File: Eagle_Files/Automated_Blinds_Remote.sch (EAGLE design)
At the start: 25 parts, among them U1 LPC1114FN28/102, U2 UA78MC

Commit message: Finished PCB design for remote control
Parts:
- added R8, R9: 10, rcl:R-US_0207/10
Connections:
- net +3V3: now also R8.2, R9.2
- net N$1: now also R8.1, R9.1
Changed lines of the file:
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@@
 <part name="+3V14" library="supply1" deviceset="+3V3" device=""/>
 <part name="POWER_SWITCH" library="DIP-SLIDE-SWITCH_3P-11.6X4.0X5.4_2.0MM_" deviceset="DIP-SLIDE-SWITCH(3P-11.6X4.0X5.4+2.0MM)" device="-EG1218"/>
+<part name="R8" library="rcl" deviceset="R-US_" device="0207/10" value="10"/>
+<part name="R9" library="rcl" deviceset="R-US_" device="0207/10" value="10"/>
 </parts>
 <sheets>
@@
 <text x="-55.88" y="73.66" size="1.778" layer="91">ACTION BUTTONS</text>
 <text x="-55.88" y="15.24" size="1.778" layer="91">SELECTION BUTTONS</text>
-<text x="78.74" y="96.52" size="1.778" layer="91">IR TRANSMITTER</text>
+<text x="68.58" y="96.52" size="1.778" layer="91">IR TRANSMITTER</text>
 </plain>
 <instances>
@@
 <instance part="+3V14" gate="G$1" x="86.36" y="91.44"/>
 <instance part="POWER_SWITCH" gate="G$1" x="22.86" y="68.58"/>
+<instance part="R8" gate="G$1" x="96.52" y="78.74" rot="MR0"/>
+<instance part="R9" gate="G$1" x="96.52" y="93.98" rot="MR0"/>
 </instances>
 <busses>
@@
 <wire x1="86.36" y1="86.36" x2="86.36" y2="88.9" width="0.1524" layer="91"/>
 <pinref part="+3V14" gate="G$1" pin="+3V3"/>
+<pinref part="R9" gate="G$1" pin="2"/>
+<wire x1="91.44" y1="86.36" x2="91.44" y2="93.98" width="0.1524" layer="91"/>
+<pinref part="R8" gate="G$1" pin="2"/>
+<wire x1="91.44" y1="86.36" x2="91.44" y2="78.74" width="0.1524" layer="91"/>
 </segment>
 </net>
@@
 <pinref part="R7" gate="G$1" pin="1"/>
 <wire x1="106.68" y1="86.36" x2="101.6" y2="86.36" width="0.1524" layer="91"/>
-</segment>
-</net>
+<pinref part="R8" gate="G$1" pin="1"/>
+<wire x1="101.6" y1="78.74" x2="101.6" y2="86.36" width="0.1524" layer="91"/>
+<pinref part="R9" gate="G$1" pin="1"/>
+<wire x1="101.6" y1="93.98" x2="101.6" y2="86.36" width="0.1524" layer="91"/>
+</segment>
+</net>

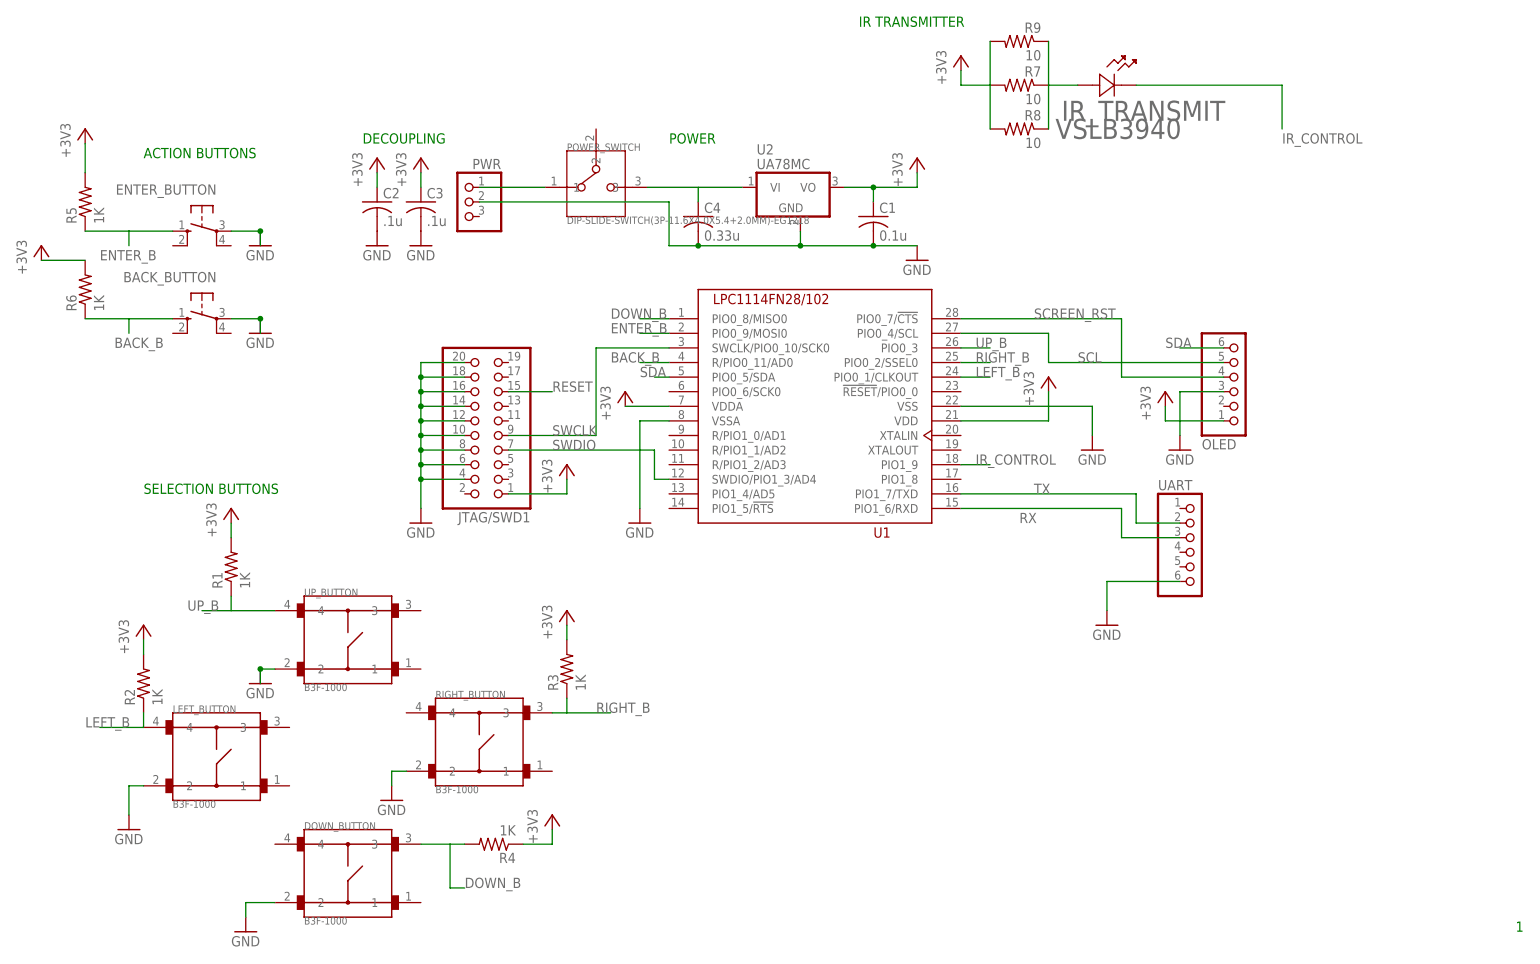
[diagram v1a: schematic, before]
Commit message: Updated value of button pull-ups in schematic
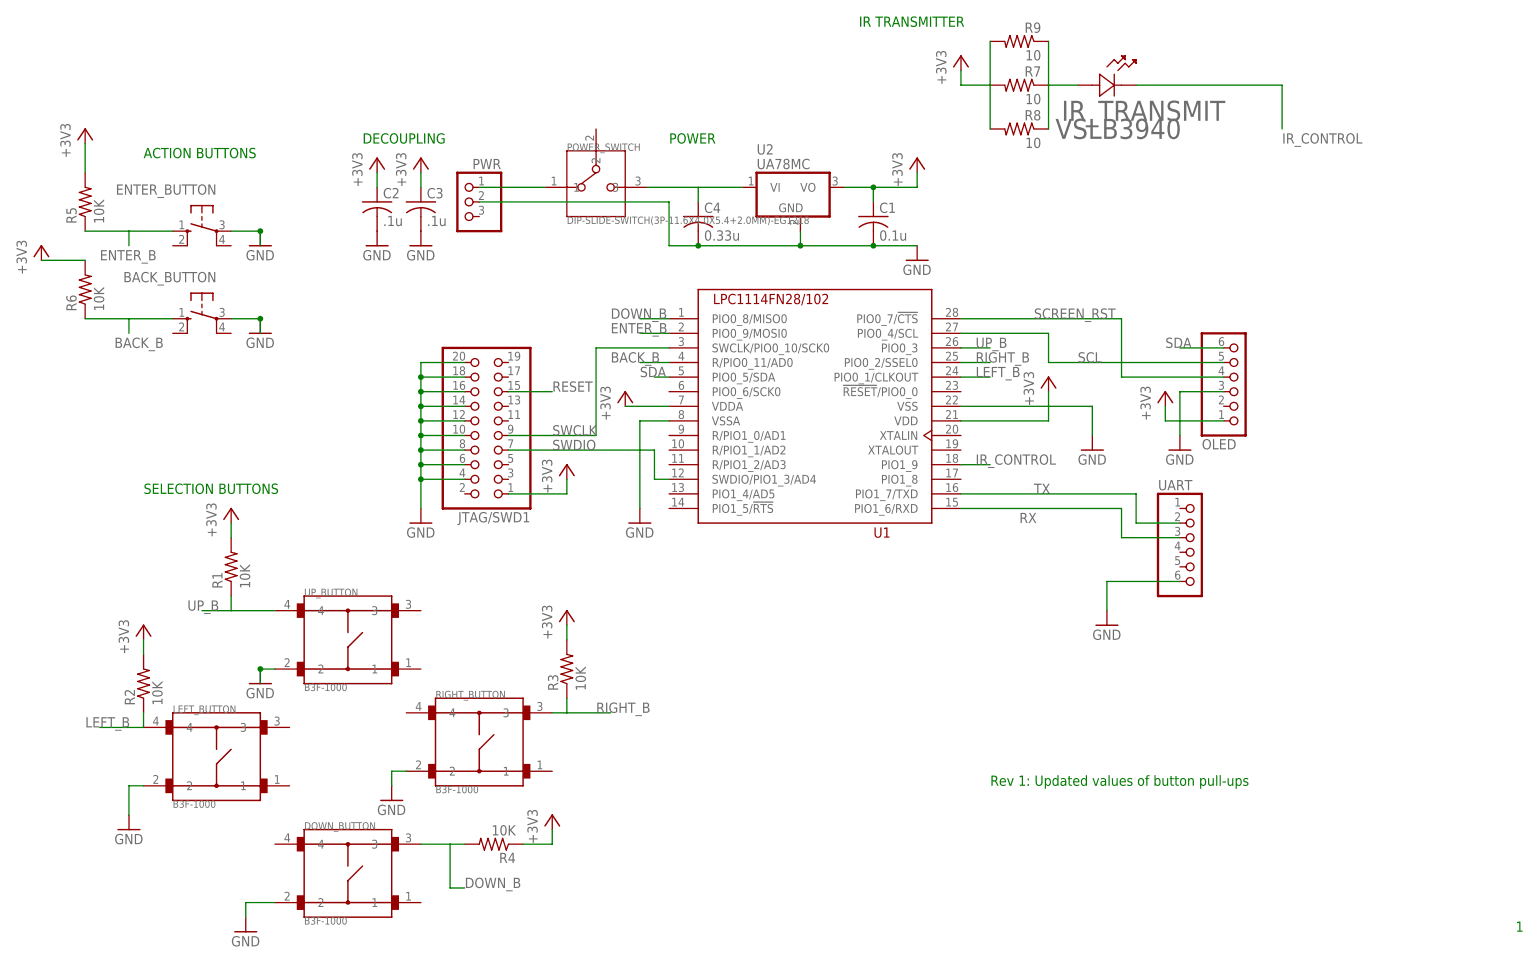
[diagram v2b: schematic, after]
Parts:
- R1, R2, R3, R4, R5, R6: value 1K -> 10K
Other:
- note added: "Rev 1: Updated values of button pull-ups"
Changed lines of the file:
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@@
 <grid distance="0.1" unitdist="inch" unit="inch" style="lines" multiple="1" display="no" altdistance="0.01" altunitdist="inch" altunit="inch"/>
 <layers>
-<layer number="1" name="Top" color="4" fill="1" visible="no" active="no"/>
-<layer number="2" name="Route2" color="1" fill="3" visible="no" active="no"/>
-<layer number="3" name="Route3" color="4" fill="3" visible="no" active="no"/>
-<layer number="4" name="Route4" color="1" fill="4" visible="no" active="no"/>
-<layer number="5" name="Route5" color="4" fill="4" visible="no" active="no"/>
-<layer number="6" name="Route6" color="1" fill="8" visible="no" active="no"/>
-<layer number="7" name="Route7" color="4" fill="8" visible="no" active="no"/>
-<layer number="8" name="Route8" color="1" fill="2" visible="no" active="no"/>
-<layer number="9" name="Route9" color="4" fill="2" visible="no" active="no"/>
-<layer number="10" name="Route10" color="1" fill="7" visible="no" active="no"/>
-<layer number="11" name="Route11" color="4" fill="7" visible="no" active="no"/>
-<layer number="12" name="Route12" color="1" fill="5" visible="no" active="no"/>
-<layer number="13" name="Route13" color="4" fill="5" visible="no" active="no"/>
-<layer number="14" name="Route14" color="1" fill="6" visible="no" active="no"/>
-<layer number="15" name="Route15" color="4" fill="6" visible="no" active="no"/>
-<layer number="16" name="Bottom" color="1" fill="1" visible="no" active="no"/>
-<layer number="17" name="Pads" color="2" fill="1" visible="no" active="no"/>
-<layer number="18" name="Vias" color="2" fill="1" visible="no" active="no"/>
-<layer number="19" name="Unrouted" color="6" fill="1" visible="no" active="no"/>
-<layer number="20" name="Dimension" color="15" fill="1" visible="no" active="no"/>
-<layer number="21" name="tPlace" color="7" fill="1" visible="no" active="no"/>
-<layer number="22" name="bPlace" color="7" fill="1" visible="no" active="no"/>
-<layer number="23" name="tOrigins" color="15" fill="1" visible="no" active="no"/>
-<layer number="24" name="bOrigins" color="15" fill="1" visible="no" active="no"/>
-<layer number="25" name="tNames" color="7" fill="1" visible="no" active="no"/>
-<layer number="26" name="bNames" color="7" fill="1" visible="no" active="no"/>
-<layer number="27" name="tValues" color="7" fill="1" visible="no" active="no"/>
-<layer number="28" name="bValues" color="7" fill="1" visible="no" active="no"/>
+<layer number="1" name="Top" color="4" fill="1" visible="yes" active="no"/>
+<layer number="2" name="Route2" color="1" fill="3" visible="yes" active="no"/>
+<layer number="3" name="Route3" color="4" fill="3" visible="yes" active="no"/>
+<layer number="4" name="Route4" color="1" fill="4" visible="yes" active="no"/>
+<layer number="5" name="Route5" color="4" fill="4" visible="yes" active="no"/>
+<layer number="6" name="Route6" color="1" fill="8" visible="yes" active="no"/>
+<layer number="7" name="Route7" color="4" fill="8" visible="yes" active="no"/>
+<layer number="8" name="Route8" color="1" fill="2" visible="yes" active="no"/>
+<layer number="9" name="Route9" color="4" fill="2" visible="yes" active="no"/>
+<layer number="10" name="Route10" color="1" fill="7" visible="yes" active="no"/>
+<layer number="11" name="Route11" color="4" fill="7" visible="yes" active="no"/>
+<layer number="12" name="Route12" color="1" fill="5" visible="yes" active="no"/>
+<layer number="13" name="Route13" color="4" fill="5" visible="yes" active="no"/>
+<layer number="14" name="Route14" color="1" fill="6" visible="yes" active="no"/>
+<layer number="15" name="Route15" color="4" fill="6" visible="yes" active="no"/>
+<layer number="16" name="Bottom" color="1" fill="1" visible="yes" active="no"/>
+<layer number="17" name="Pads" color="2" fill="1" visible="yes" active="no"/>
+<layer number="18" name="Vias" color="2" fill="1" visible="yes" active="no"/>
+<layer number="19" name="Unrouted" color="6" fill="1" visible="yes" active="no"/>
+<layer number="20" name="Dimension" color="15" fill="1" visible="yes" active="no"/>
+<layer number="21" name="tPlace" color="7" fill="1" visible="yes" active="no"/>
+<layer number="22" name="bPlace" color="7" fill="1" visible="yes" active="no"/>
+<layer number="23" name="tOrigins" color="15" fill="1" visible="yes" active="no"/>
+<layer number="24" name="bOrigins" color="15" fill="1" visible="yes" active="no"/>
+<layer number="25" name="tNames" color="7" fill="1" visible="yes" active="no"/>
+<layer number="26" name="bNames" color="7" fill="1" visible="yes" active="no"/>
+<layer number="27" name="tValues" color="7" fill="1" visible="yes" active="no"/>
+<layer number="28" name="bValues" color="7" fill="1" visible="yes" active="no"/>
 <layer number="29" name="tStop" color="7" fill="3" visible="no" active="no"/>
 <layer number="30" name="bStop" color="7" fill="6" visible="no" active="no"/>
@@
 <layer number="35" name="tGlue" color="7" fill="4" visible="no" active="no"/>
 <layer number="36" name="bGlue" color="7" fill="5" visible="no" active="no"/>
-<layer number="37" name="tTest" color="7" fill="1" visible="no" active="no"/>
-<layer number="38" name="bTest" color="7" fill="1" visible="no" active="no"/>
+<layer number="37" name="tTest" color="7" fill="1" visible="yes" active="no"/>
+<layer number="38" name="bTest" color="7" fill="1" visible="yes" active="no"/>
 <layer number="39" name="tKeepout" color="4" fill="11" visible="no" active="no"/>
 <layer number="40" name="bKeepout" color="1" fill="11" visible="no" active="no"/>
@@
 <layer number="44" name="Drills" color="7" fill="1" visible="no" active="no"/>
 <layer number="45" name="Holes" color="7" fill="1" visible="no" active="no"/>
-<layer number="46" name="Milling" color="3" fill="1" visible="no" active="no"/>
-<layer number="47" name="Measures" color="7" fill="1" visible="no" active="no"/>
-<layer number="48" name="Document" color="7" fill="1" visible="no" active="no"/>
-<layer number="49" name="Reference" color="7" fill="1" visible="no" active="no"/>
-<layer number="50" name="dxf" color="7" fill="1" visible="no" active="no"/>
-<layer number="51" name="tDocu" color="7" fill="1" visible="no" active="no"/>
-<layer number="52" name="bDocu" color="7" fill="1" visible="no" active="no"/>
-<layer number="53" name="tGND_GNDA" color="7" fill="9" visible="no" active="no"/>
-<layer number="54" name="bGND_GNDA" color="1" fill="9" visible="no" active="no"/>
-<layer number="56" name="wert" color="7" fill="1" visible="no" active="no"/>
+<layer number="46" name="Milling" color="3" fill="1" visible="yes" active="no"/>
+<layer number="47" name="Measures" color="7" fill="1" visible="yes" active="no"/>
+<layer number="48" name="Document" color="7" fill="1" visible="yes" active="no"/>
+<layer number="49" name="Reference" color="7" fill="1" visible="yes" active="no"/>
+<layer number="50" name="dxf" color="7" fill="1" visible="yes" active="no"/>
+<layer number="51" name="tDocu" color="7" fill="1" visible="yes" active="no"/>
+<layer number="52" name="bDocu" color="7" fill="1" visible="yes" active="no"/>
+<layer number="53" name="tGND_GNDA" color="7" fill="9" visible="yes" active="no"/>
+<layer number="54" name="bGND_GNDA" color="1" fill="9" visible="yes" active="no"/>
+<layer number="56" name="wert" color="7" fill="1" visible="yes" active="no"/>
 <layer number="90" name="Modules" color="5" fill="1" visible="yes" active="yes"/>
 <layer number="91" name="Nets" color="2" fill="1" visible="yes" active="yes"/>
@@
 <part name="GND11" library="supply1" deviceset="GND" device=""/>
 <part name="GND12" library="supply1" deviceset="GND" device=""/>
-<part name="R1" library="rcl" deviceset="R-US_" device="0207/10" value="1K"/>
-<part name="R2" library="rcl" deviceset="R-US_" device="0207/10" value="1K"/>
-<part name="R3" library="rcl" deviceset="R-US_" device="0207/10" value="1K"/>
-<part name="R4" library="rcl" deviceset="R-US_" device="0207/10" value="1K"/>
+<part name="R1" library="rcl" deviceset="R-US_" device="0207/10" value="10K"/>
+<part name="R2" library="rcl" deviceset="R-US_" device="0207/10" value="10K"/>
+<part name="R3" library="rcl" deviceset="R-US_" device="0207/10" value="10K"/>
+<part name="R4" library="rcl" deviceset="R-US_" device="0207/10" value="10K"/>
 <part name="+3V8" library="supply1" deviceset="+3V3" device=""/>
 <part name="+3V9" library="supply1" deviceset="+3V3" device=""/>
@@
 <part name="ENTER_BUTTON" library="switch-omron" deviceset="40/XX" device=""/>
 <part name="BACK_BUTTON" library="switch-omron" deviceset="40/XX" device=""/>
-<part name="R5" library="rcl" deviceset="R-US_" device="0207/10" value="1K"/>
+<part name="R5" library="rcl" deviceset="R-US_" device="0207/10" value="10K"/>
 <part name="+3V12" library="supply1" deviceset="+3V3" device=""/>
 <part name="GND13" library="supply1" deviceset="GND" device=""/>
 <part name="GND14" library="supply1" deviceset="GND" device=""/>
-<part name="R6" library="rcl" deviceset="R-US_" device="0207/10" value="1K"/>
+<part name="R6" library="rcl" deviceset="R-US_" device="0207/10" value="10K"/>
 <part name="+3V13" library="supply1" deviceset="+3V3" device=""/>
 <part name="IR_TRANSMIT" library="VSLB3940" deviceset="VSLB3940" device=""/>
@@
 <text x="-55.88" y="15.24" size="1.778" layer="91">SELECTION BUTTONS</text>
 <text x="68.58" y="96.52" size="1.778" layer="91">IR TRANSMITTER</text>
+<text x="91.44" y="-35.56" size="1.778" layer="91">Rev 1: Updated values of button pull-ups</text>
 </plain>
 <instances>
